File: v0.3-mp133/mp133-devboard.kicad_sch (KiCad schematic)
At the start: 146 parts, among them CON1 microSDCon_SMT_104031-0811, J1 Pins_02x40_P0.4mm_W3.0mm_SMT, J2 Pins_02x40_P0.4mm_W3.0mm_SMT, J3 USB-C_Receptacle_Molex_217179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, J4 Pins_02x04_RightAngle_P2.54mm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, J5 Conn_01x02, J6 Pins_02x05_P1.27mm_SMT, U13 NCP51460SN33, U14 DDR3L-RAM-4Gb_MT41K256M16TW, U15 AP6230xZ6, U16 AP6230xZ6, U17 AP6230xZ6, U18 TAR5S33, U19 TAR5S33, U2 STM32MP133DAF, U20 AP2411SN, U21 AP6230xZ6, U3 USBLC6-2SC6, U5 NORFLASH_W25Q128JV, X2 24MHz_8pF_2x1.6mm

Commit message: WIP Routing
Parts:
- added C1: 1uF_0201_4V, 4ms_Capacitor:C_0201, symbol 4ms_Capacitor:1uF_0201_4V
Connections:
- net GND: now also C1.2
- net PB1: now also J2.35 (Pin_35), J2.36 (Pin_36)
- net VDD: now also C1.1
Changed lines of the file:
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@@
 	(text "ADC-5"
 		(exclude_from_sim no)
-		(at 162.814 111.76 0)
+		(at 179.324 110.49 0)
 		(effects
 			(font
@@
 	)
 	(junction
+		(at 585.47 570.23)
+		(diameter 0)
+		(color 0 0 0 0)
+	)
+	(junction
 		(at 201.93 158.75)
 		(diameter 0)
@@
 	)
 	(junction
+		(at 585.47 575.31)
+		(diameter 0)
+		(color 0 0 0 0)
+	)
+	(junction
 		(at 398.78 279.4)
 		(diameter 0)
@@
 	(wire
 		(pts
+			(xy 585.47 575.31) (xy 594.36 575.31)
+		)
+		(stroke
+			(width 0)
+			(type default)
+		)
+	)
+	(wire
+		(pts
 			(xy 528.32 402.59) (xy 528.32 405.13)
 		)
@@
 	(wire
 		(pts
+			(xy 585.47 570.23) (xy 594.36 570.23)
+		)
+		(stroke
+			(width 0)
+			(type default)
+		)
+	)
+	(wire
+		(pts
 			(xy 434.34 220.98) (xy 458.47 220.98)
 		)
@@
 	)
 	(label "PB1"
-		(at 157.48 111.76 0)
+		(at 173.99 110.49 0)
 		(effects
 			(font
@@
 					(unit 1)
 				)
+			)
+		)
+	)
+	(symbol
+		(lib_id "4ms_Capacitor:1uF_0201_4V")
+		(at 594.36 572.77 0)
+		(unit 1)
+		(exclude_from_sim no)
+		(in_bom yes)
+		(on_board yes)
+		(dnp no)
+		(fields_autoplaced yes)
+		(property "Reference" "C1"
+			(at 596.6841 571.7523 0)
+			(effects
+				(font
+					(size 1.27 1.27)
+				)
+				(justify left)
+			)
+		)
+		(property "Value" "1uF_0201_4V"
+			(at 594.36 568.96 0)
+			(effects
+				(font
+					(size 1.27 1.27)
+				)
+				(hide yes)
+			)
+		)
+		(property "Footprint" "4ms_Capacitor:C_0201"
+			(at 591.82 577.85 0)
+			(effects
+				(font
+					(size 1.27 1.27)
+				)
+				(justify left)
+				(hide yes)
+			)
+		)
+		(property "Datasheet" ""
+			(at 594.36 572.77 0)
+			(effects
+				(font
+					(size 1.27 1.27)
+				)
+				(hide yes)
+			)
+		)
+		(property "Description" ""
+			(at 594.36 572.77 0)
+			(effects
+				(font
+					(size 1.27 1.27)
+				)
+			)
+		)
+		(property "Specifications" "1uF, Min. 4V 10%, X7R or X5R or X6S or similar"
+			(at 591.82 580.644 0)
+			(effects
+				(font
+					(size 1.27 1.27)
+				)
+				(justify left)
+				(hide yes)
+			)
+		)
+		(property "Display" "1uF"
+			(at 596.6841 573.8003 0)
+			(effects
+				(font
+					(size 1.27 1.27)
+				)
+				(justify left)
+			)
+		)
+		(property "Manufacturer" "Yageo"
+			(at 595.63 586.74 0)
+			(effects
+				(font
+					(size 1.27 1.27)
+				)
+				(hide yes)
+			)
+		)
+		(property "Part Number" "CC0201MRX5R5BB105"
+			(at 601.98 589.28 0)
+			(effects
+				(font
+					(size 1.27 1.27)
+				)
+				(hide yes)
+			)
+		)
+		(property "JLCPCB ID" "C272877"
+			(at 595.63 585.47 0)
+			(effects
+				(font
+					(size 1.27 1.27)
+				)
+				(hide yes)
+			)
+		)
+		(property "Manufacturer 2" "Murata"
+			(at 591.82 582.168 0)
+			(effects
+				(font
+					(size 1.27 1.27)
+				)
+				(justify left)
+				(hide yes)
+			)
+		)
+		(property "Part Number 2" "GRM033D70G105ME01D"
+			(at 591.82 583.692 0)
+			(effects
+				(font
+					(size 1.27 1.27)
+				)
+				(justify left)
+				(hide yes)
+			)
+		)
+		(property "Production Stage" "A"
+			(at 591.82 589.28 0)
+			(effects
+				(font
+					(size 1.27 1.27)
+				)
+				(justify left)
+				(hide yes)
+			)
+		)
+		(property "Alt Part Number" ""
+			(at 594.36 572.77 0)
+			(effects
+				(font
+					(size 1.27 1.27)
+				)
+				(hide yes)
+			)
+		)
+		(pin "1"
+		)
+		(pin "2"
+		)
+		(instances
+			(project "mp133-devboard"
+				(path "/64ec1a6b-f4f9-4414-abbd-a05816451f08"
+					(reference "C1")
+					(unit 1)
+				)

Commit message: WIP routing
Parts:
- removed C30: 100nF_0402_16V, 4ms_Capacitor:C_0402, symbol 4ms_Capacitor:100nF_0402_16V
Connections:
- net GND: now also U2.U3 (VSS_ANA)
- net GNDADC: no longer U2.U3 (VSS_ANA)
- net PA0: now also J2.31 (Pin_31), J2.32 (Pin_32); no longer J2.29 (Pin_29), J2.30 (Pin_30)
- net PA1: now also J2.33 (Pin_33), J2.34 (Pin_34); no longer J2.31 (Pin_31), J2.32 (Pin_32)
- net PA2: now also J2.35 (Pin_35), J2.36 (Pin_36); no longer J2.33 (Pin_33), J2.34 (Pin_34)
- net PA4: now also J2.41 (Pin_41), J2.42 (Pin_42); no longer J2.37 (Pin_37), J2.38 (Pin_38)
- net PA5: now also J2.37 (Pin_37), J2.38 (Pin_38); no longer J2.39 (Pin_39), J2.40 (Pin_40)
- net PA7: now also J2.29 (Pin_29), J2.30 (Pin_30); no longer J2.43 (Pin_43), J2.44 (Pin_44)
- net PB0: no longer J2.61 (Pin_61), J2.62 (Pin_62)
- net PB1: now also J2.47 (Pin_47), J2.48 (Pin_48); no longer J2.35 (Pin_35), J2.36 (Pin_36)
- net PC0: no longer J2.41 (Pin_41), J2.42 (Pin_42)
- net PC1: now also J2.49 (Pin_49), J2.50 (Pin_50); no longer J2.45 (Pin_45), J2.46 (Pin_46)
- net PC2: now also J2.61 (Pin_61), J2.62 (Pin_62); no longer J2.47 (Pin_47), J2.48 (Pin_48)
- net PC4: now also J2.43 (Pin_43), J2.44 (Pin_44); no longer J2.49 (Pin_49), J2.50 (Pin_50)
- net PC5: now also J2.45 (Pin_45), J2.46 (Pin_46); no longer J2.51 (Pin_51), J2.52 (Pin_52)
- net PF11: now also J2.39 (Pin_39), J2.40 (Pin_40)
- net PG13: now also J2.51 (Pin_51), J2.52 (Pin_52)
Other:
- note removed: "Can swap ADC pins including these:"

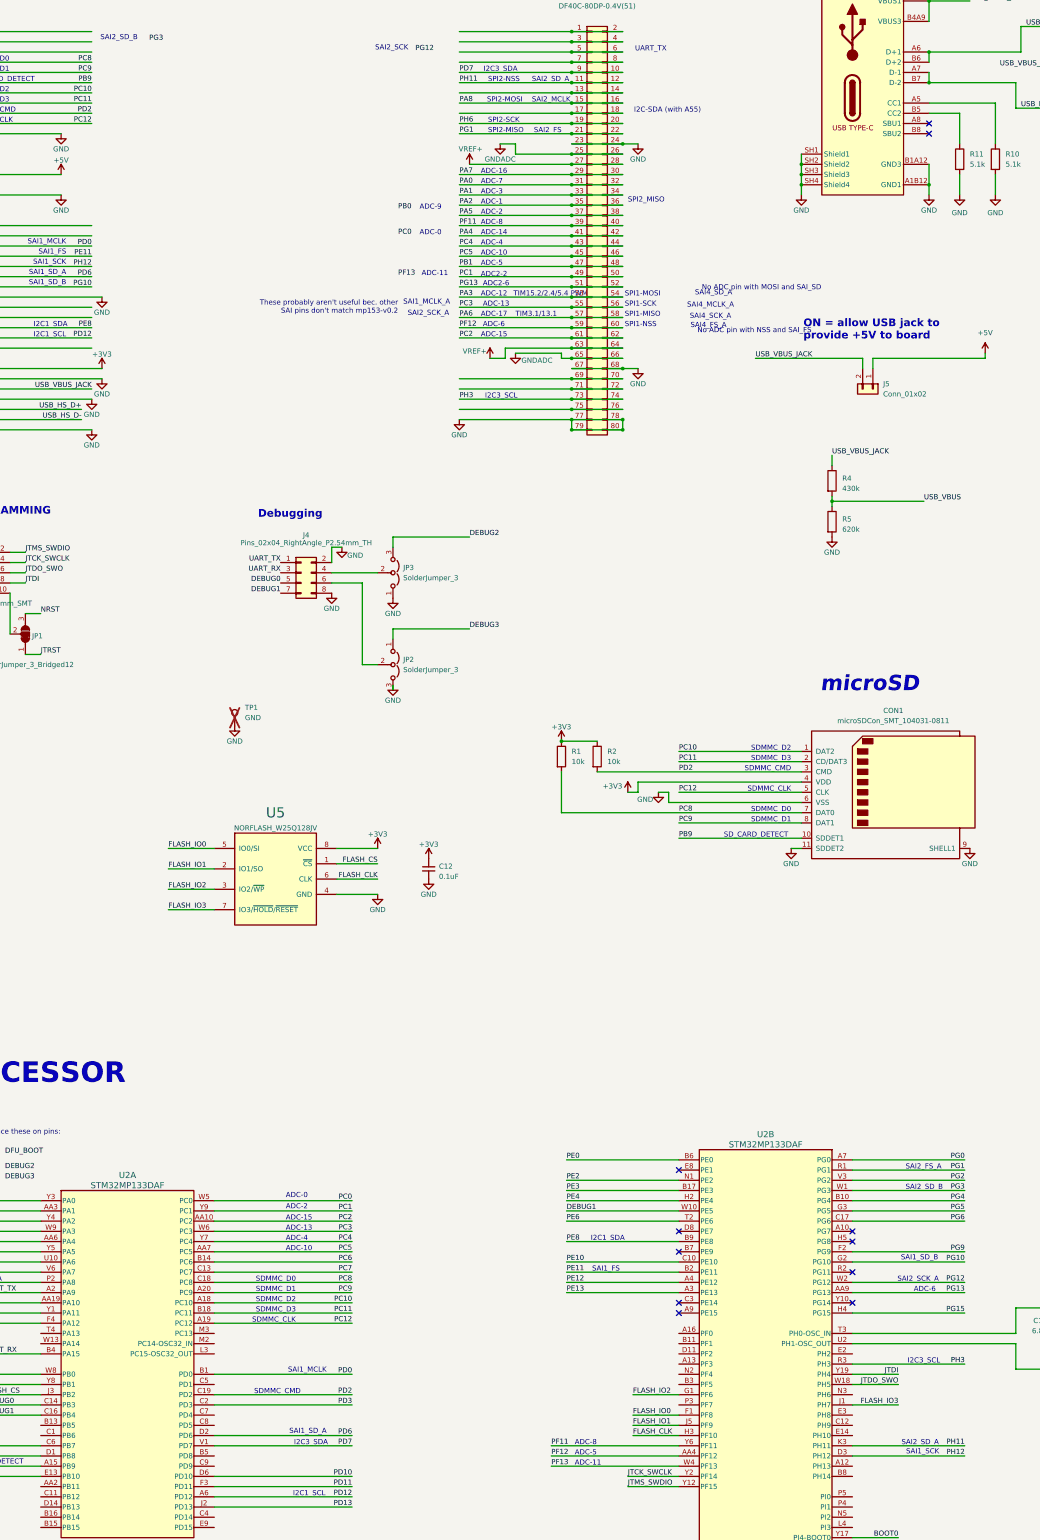
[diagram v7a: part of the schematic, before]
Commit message: mp133: WIP routing and pin assignment
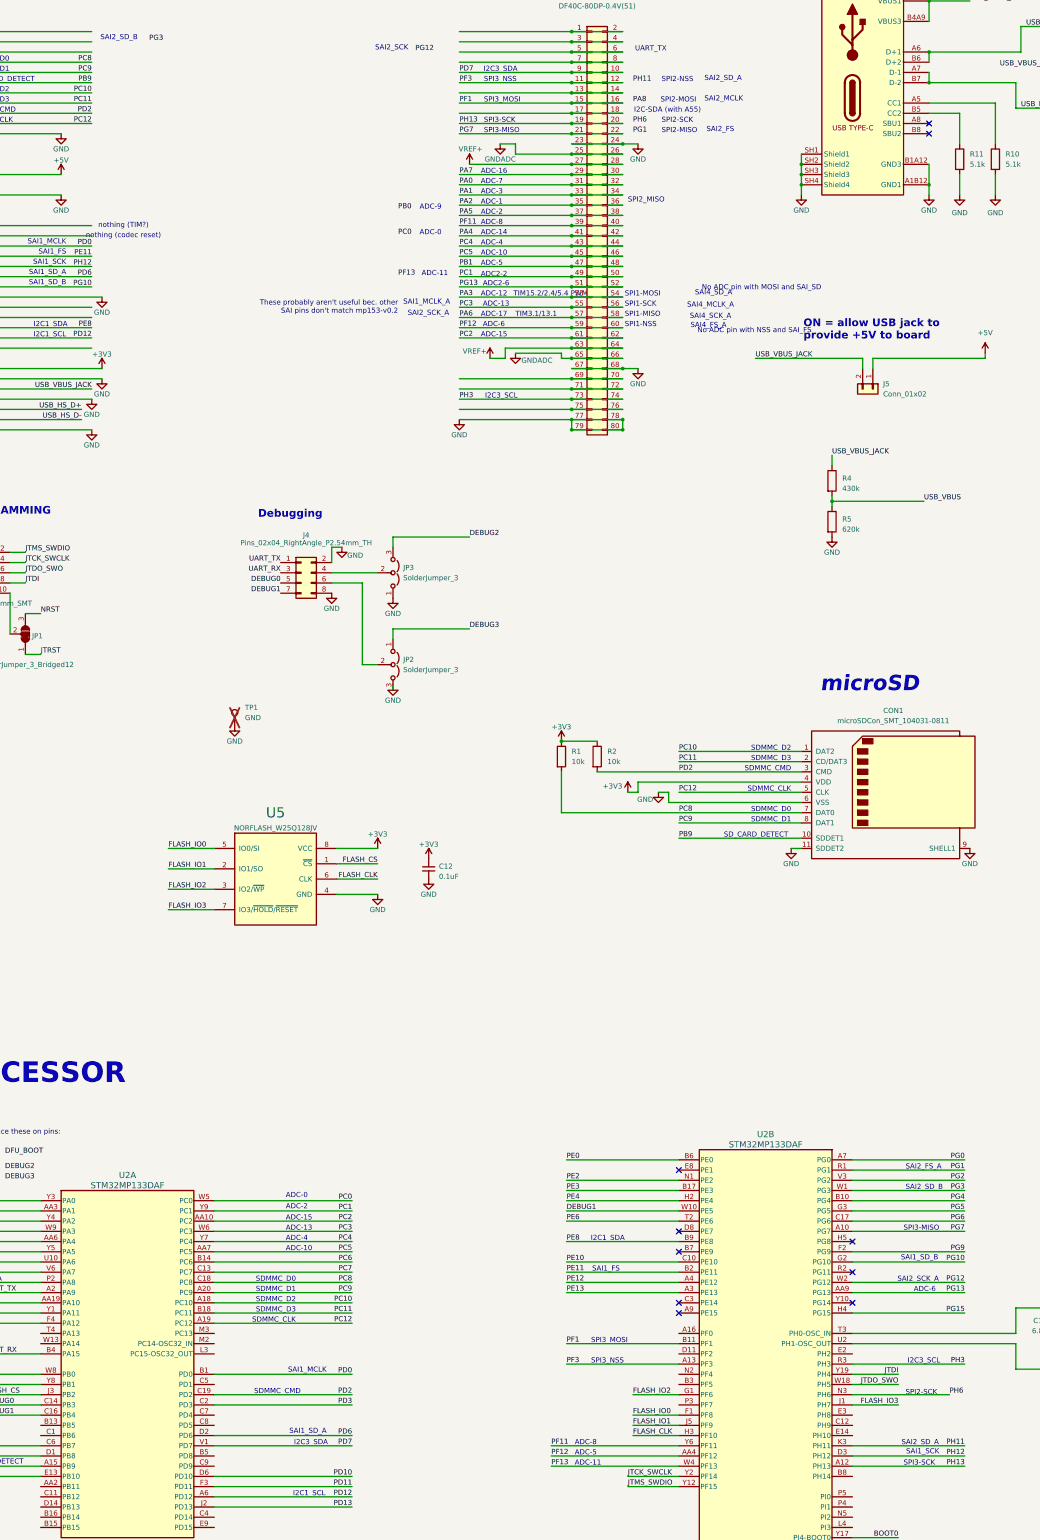
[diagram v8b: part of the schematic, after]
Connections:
- net PA8: no longer J2.15 (Pin_15), J2.16 (Pin_16)
- net PG1: no longer J2.21 (Pin_21), J2.22 (Pin_22)
- net PH11: no longer J2.11 (Pin_11), J2.12 (Pin_12)
- net PH6: now also U2.N3 (PH6); no longer J2.19 (Pin_19), J2.20 (Pin_20)
- net PG7: now reaches U2.A10 (PG7)
- net PG7: now also J2.21 (Pin_21), J2.22 (Pin_22)
- net PH13: now reaches U2.A12 (PH13)
- net PH13: now also J2.19 (Pin_19), J2.20 (Pin_20)
- net PF3: now reaches U2.A13 (PF3)
- net PF3: now also J2.11 (Pin_11), J2.12 (Pin_12)
- net PF1: now reaches U2.B11 (PF1)
- net PF1: now also J2.15 (Pin_15), J2.16 (Pin_16)
- no-connect marks 24 -> 23
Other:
- note added: "SPI3-MISO"
- note added: "SPI3-SCK"
- note added: "nothing (TIM?)"
- note added: "nothing (codec reset)"
